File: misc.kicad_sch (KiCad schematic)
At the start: 24 parts, among them U7 NTS0102_TSSOP, U8 NTS0102_TSSOP, Y1 Oscillator_25MHz_511ABA25M000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, Y2 Resonator_50MHz_XRCGE

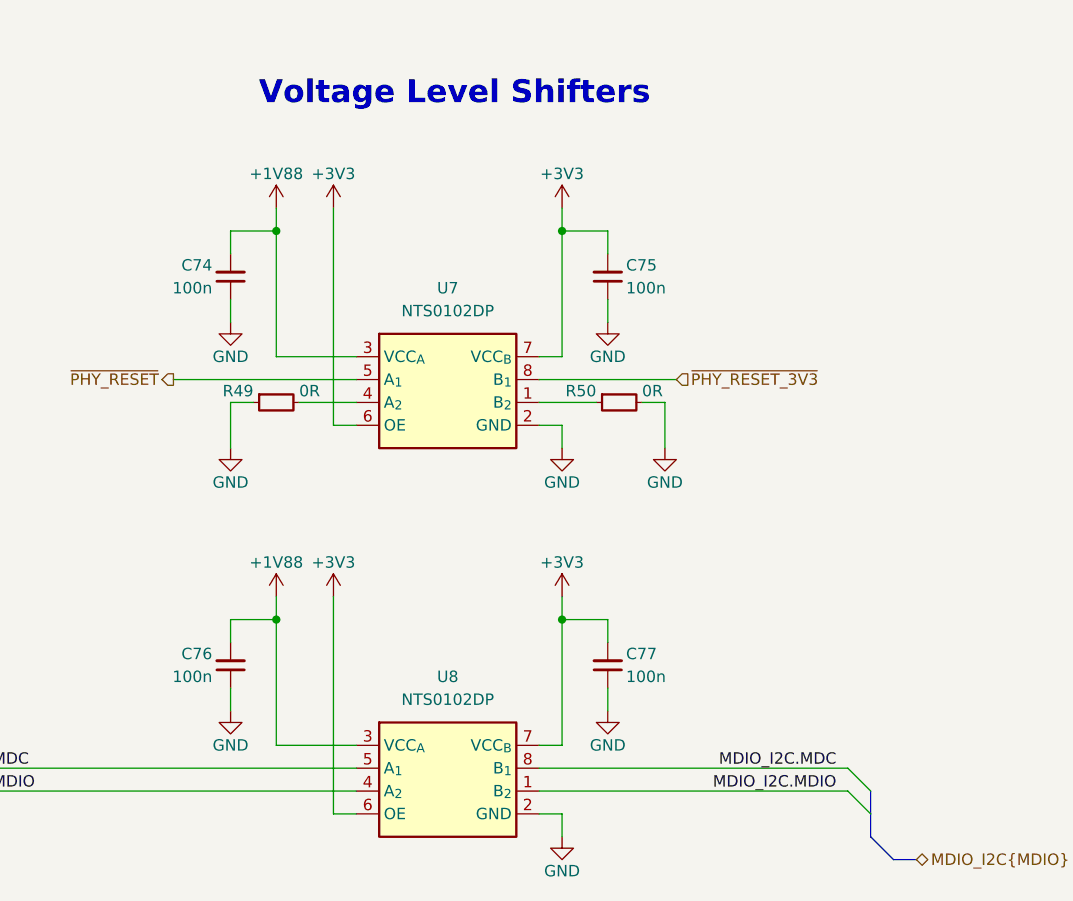
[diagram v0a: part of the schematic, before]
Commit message: [#86617] Power U10 from OCuLink, remove JTAG sheet pin, fix I2C cross
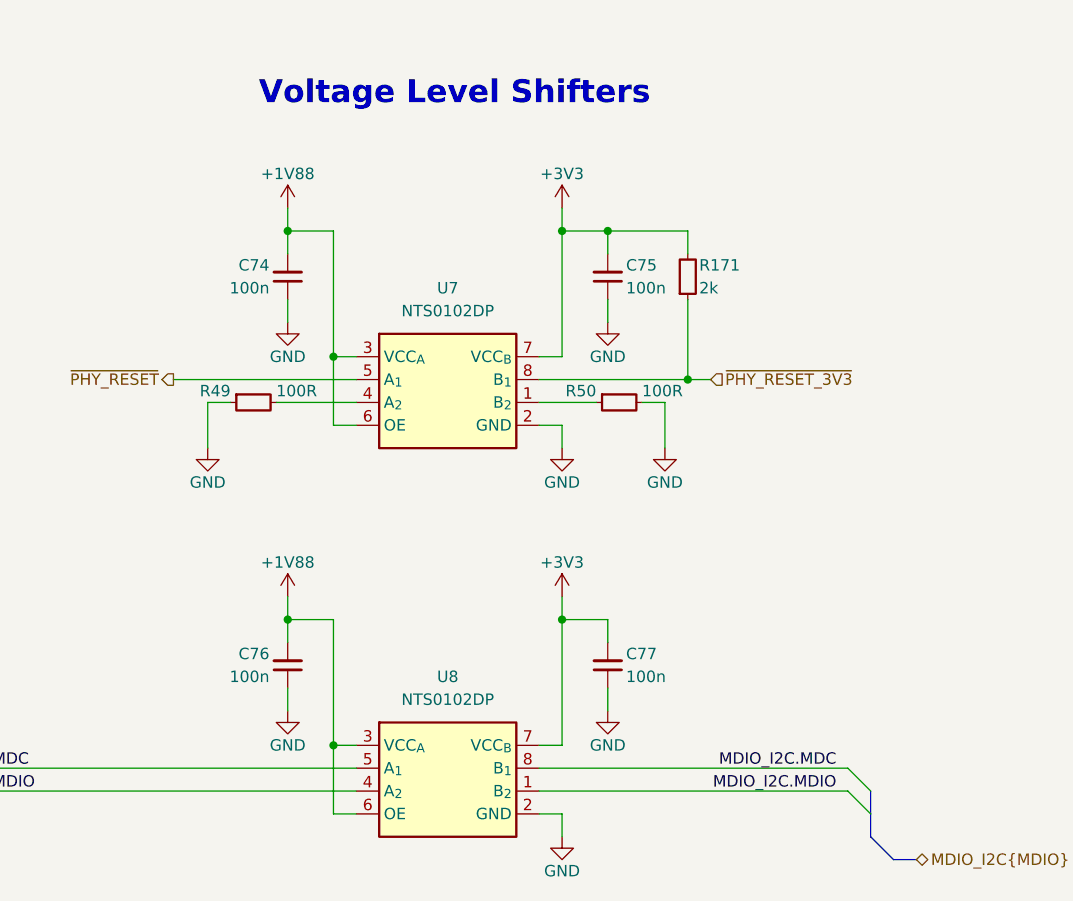
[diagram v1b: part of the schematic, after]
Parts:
- removed R49, R50: R_0R_0402, antmicro-footprints:R_0402_1005Metric, symbol antmicroResistors0402:R_0R_0402
- added R171: R_2k_0402, antmicro-footprints:R_0402_1005Metric, symbol antmicroResistors0402:R_2k_0402
- added R49, R50: R_100R_0402, antmicro-footprints:R_0402_1005Metric, symbol antmicroResistors0402:R_100R_0402
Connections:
- net +1V88: now also U7.6 (OE), U8.6 (OE)
- net +3V3: now also R171.2; no longer U7.6 (OE), U8.6 (OE)
- net GND: now also R49.1, R50.2
- net ~{PHY_RESET_3V3}: now also R171.1
- net at U7.4 (A_{2}): now also R49.2
- net at U7.1 (B_{2}): now also R50.1
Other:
- moved on the sheet: C74, C76
